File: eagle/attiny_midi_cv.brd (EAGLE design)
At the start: 100.9 x 80.9 mm, 26 parts, among them IC1 TL072P, Q518 2N3904, U2 TINY45-20-DIP

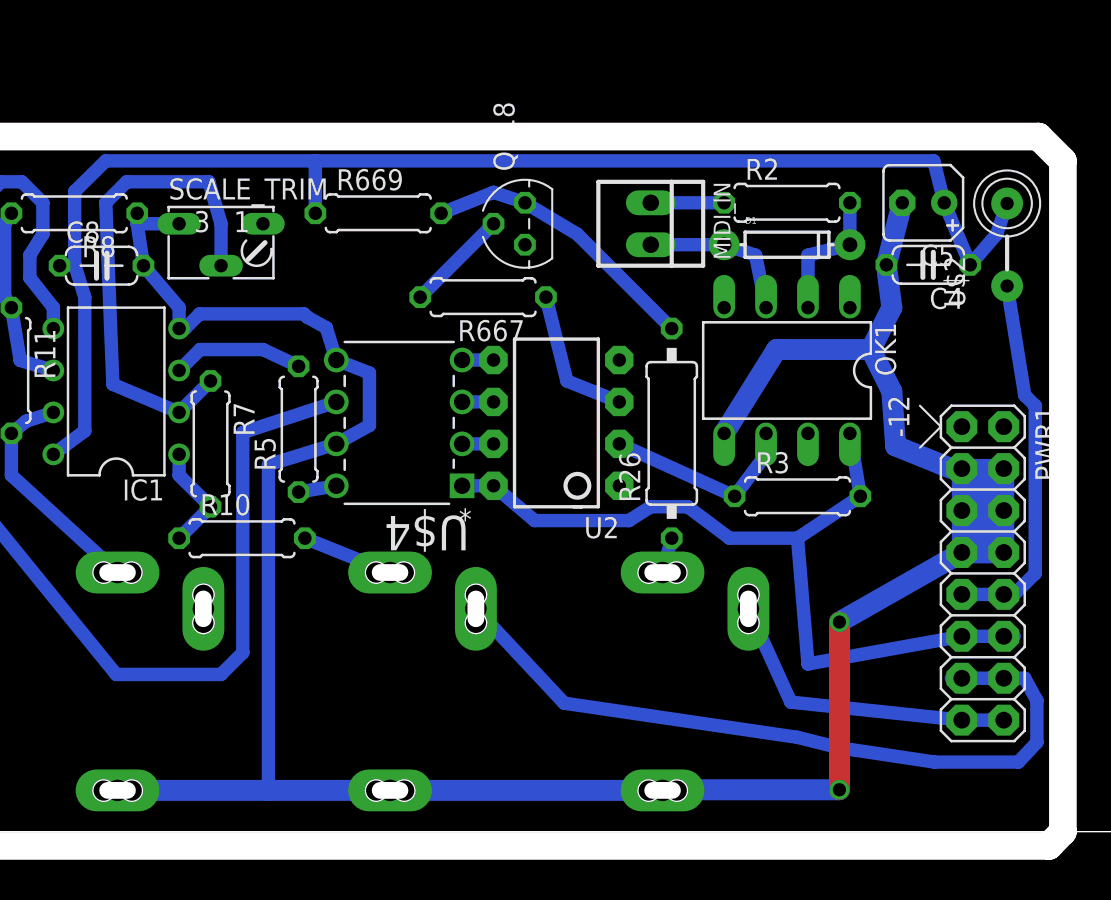
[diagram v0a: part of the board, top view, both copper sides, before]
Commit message: fixed brd and getting channel from eeprom
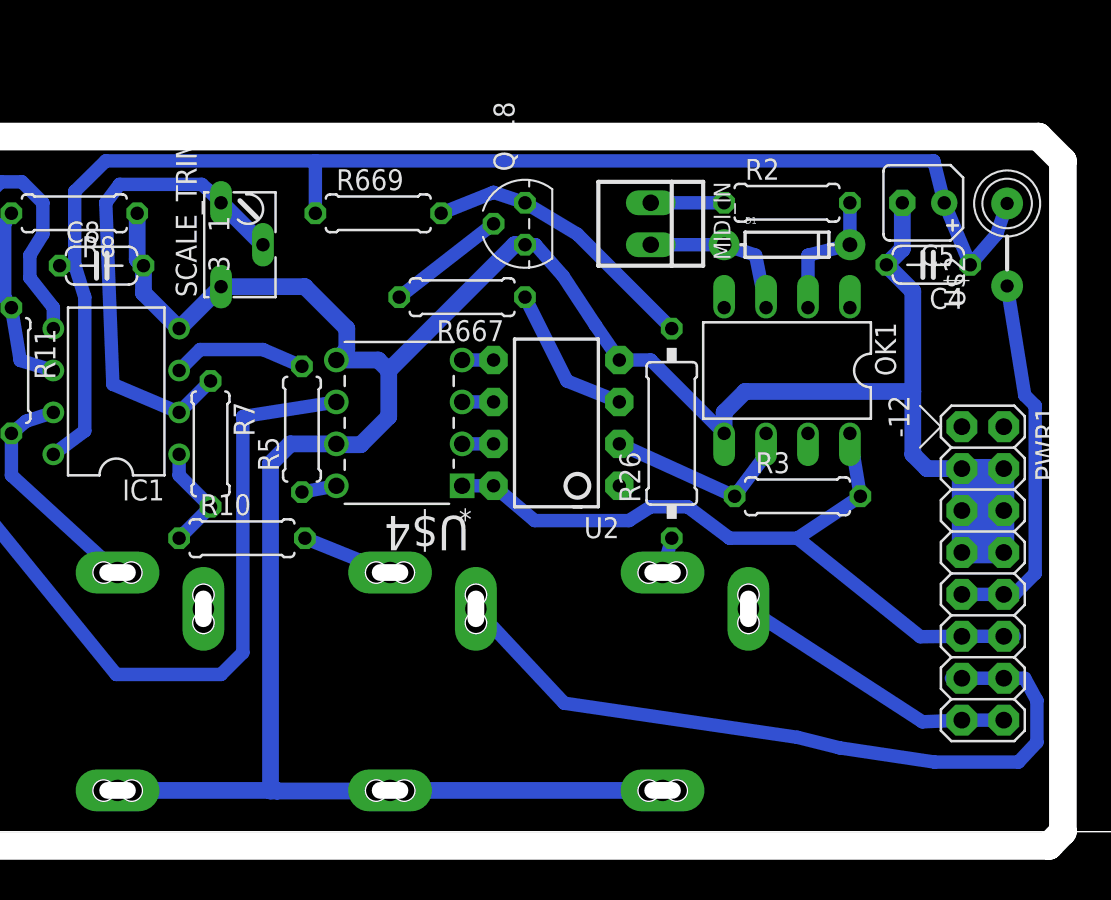
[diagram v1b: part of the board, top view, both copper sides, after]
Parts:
- moved R667 1.27 mm to (29.8, 32.4)
- moved SCALE_TRIM 1.27 mm to (15.2, 35.6), turned to 90 degrees
- moved R5 0.20 mm to (20.1, 24.4)
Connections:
- removed net N$10: C4.2, C5.-, C8.2, GATE.P$1, IC1.4, OK1.5, PITCH.P$1, PWR1.3, PWR1.4, PWR1.5, PWR1.6, PWR1.7, PWR1.8, R8.1, SCALE_TRIM.E, U$4.5, U$4.7, VEL.P$1
- net GND: now also C4.2, C5.-, C8.2, GATE.P$1, IC1.4, OK1.5, PITCH.P$1, PWR1.3, PWR1.4, PWR1.5, PWR1.6, PWR1.7, PWR1.8, R8.1, SCALE_TRIM.E, U$4.5, U$4.7, VEL.P$1
- net N$12: now also SCALE_TRIM.A
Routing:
- net GND: track 0.00 -> 164.8 mm
- net N$10: track 160.2 -> 0.00 mm, vias 2 -> 0
- net +5V: track 50.7 -> 45.6 mm
- net N$31: track 19.2 -> 17.5 mm
- net N$21: track 6.29 -> 7.24 mm
- net N$14: track 72.2 -> 73.0 mm
